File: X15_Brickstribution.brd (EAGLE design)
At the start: 152.4 x 76.2 mm, 87 parts, among them J1 IPL1-104-01-X-S-K, Q1 310mA/60V/1.6Ω, U5 IC_L4970A, U6 DIODE_STPS1545CT, U7 IC_L4970A, U8 DIODE_STPS1545CT

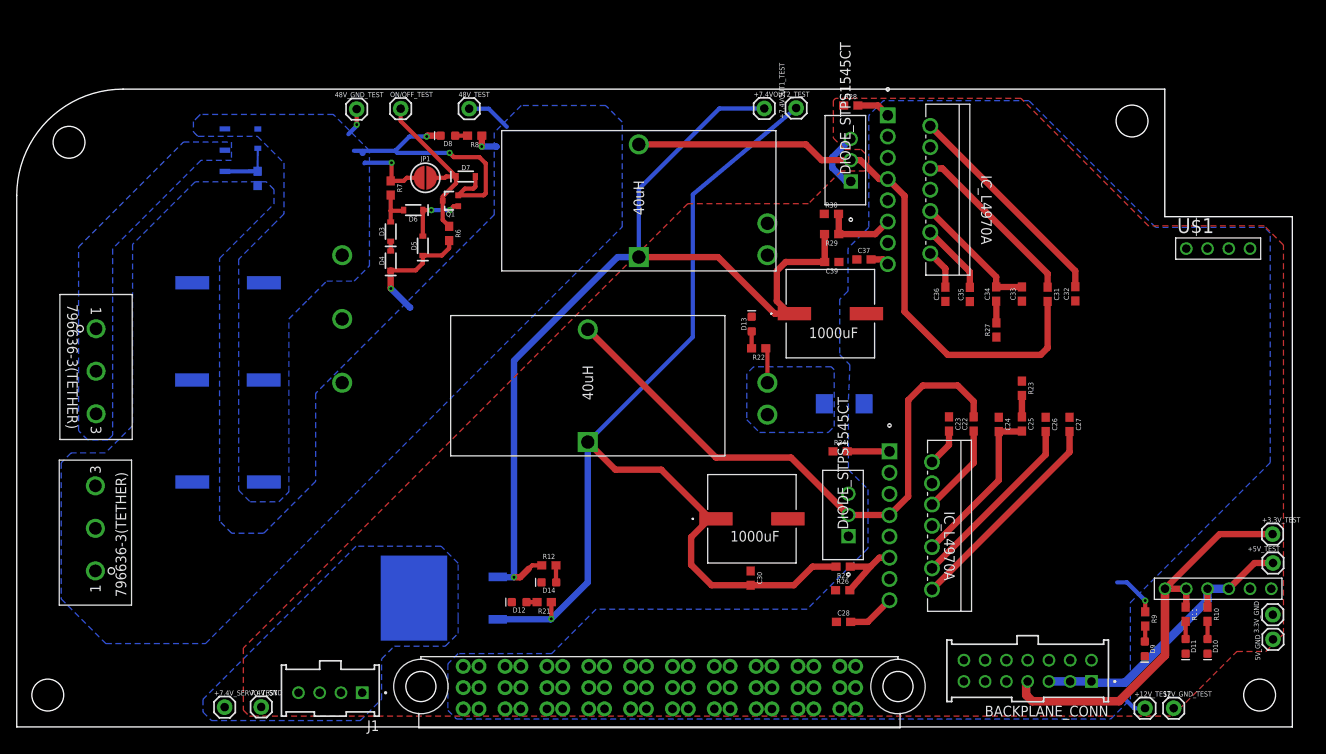
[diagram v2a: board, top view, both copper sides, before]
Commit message: Changed polygons and connections to reference voltage
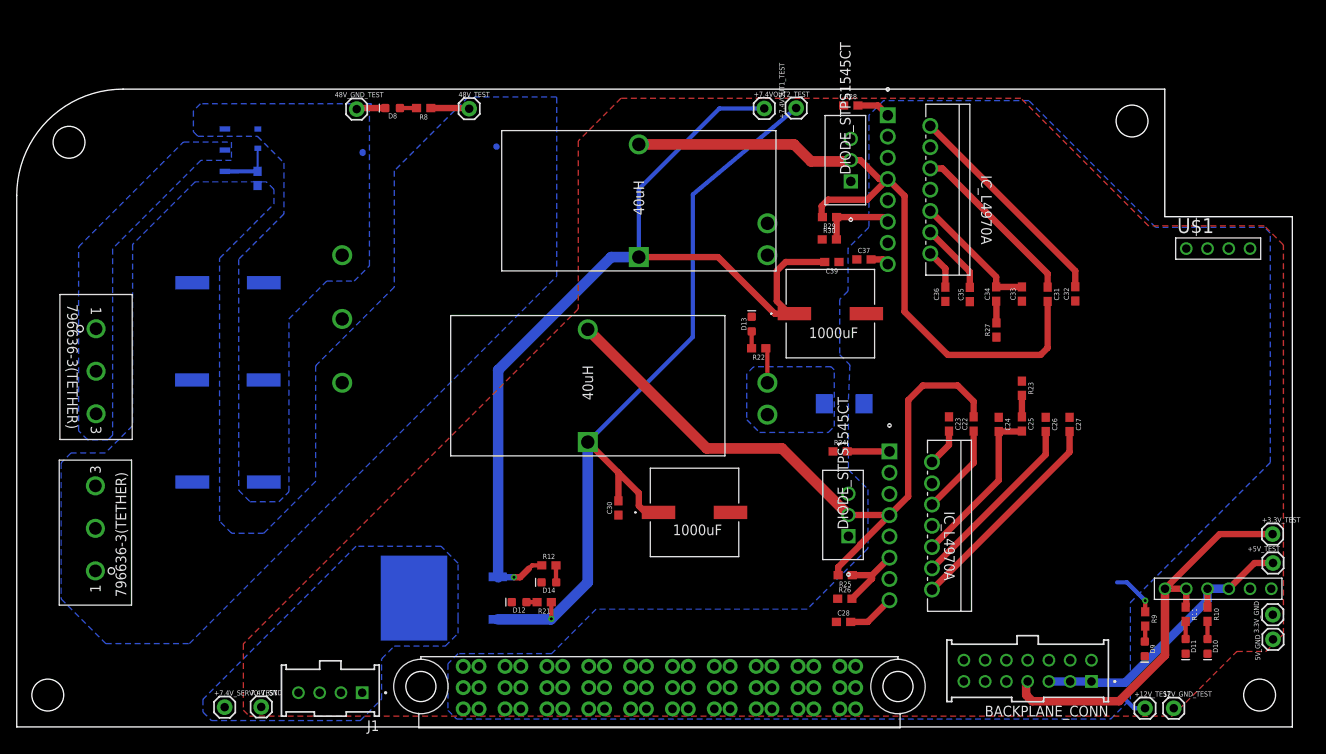
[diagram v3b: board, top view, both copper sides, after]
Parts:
- removed D3, D4: 19V, SparkFun-DiscreteSemi:SOD-323
- removed D5, D6: 250mA/100V, SparkFun-DiscreteSemi:SOD-323
- removed D7: 3.6V, SparkFun-DiscreteSemi:SOD-323
- removed JP1: JUMPER-SMT_2_NO_SILK_ROUND, SparkFun-Jumpers:SMT-JUMPER_2_NO_SILK_ROUND
- removed ON/OFF_TEST: (no value), SparkFun-Connectors:1X01
- removed Q1: 310mA/60V/1.6Ω, SparkFun-DiscreteSemi:SOT323
- removed R6: 10k, SparkFun-Resistors:0603
- removed R7: 1M, SparkFun-Resistors:0603
- moved C30 17.9 mm to (72.0, 26.2), turned to 90 degrees
- moved D8 7.38 mm to (45.0, 73.9)
- moved R8 6.93 mm to (48.7, 73.9)
- moved C29 6.90 mm to (81.1, 25.6)
- moved R30 3.06 mm to (97.2, 58.2)
- moved R29 2.05 mm to (97.2, 60.9)
- moved R25 1.05 mm to (99.1, 18.1)
- moved R26 1.05 mm to (99.0, 15.3)
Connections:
- removed net N$5: D3.C, D4.A
- removed net N$6: D3.A, D6.A, R7.2
- removed net N$7: D5.A, D6.C, Q1.1
- removed net ON/OFF: D7.C, JP1.2, ON/OFF_TEST.1, Q1.3, R6.1
- net +48V: no longer D4.C, D5.C, R6.2
- net 48V_GND: no longer D7.A, JP1.1, Q1.2, R7.1
- net OUT1: now also R25.2
- net OUT2: now also R29.2
- net VOUT1: no longer R25.2
- net VOUT2: no longer R29.2
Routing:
- net 48V_GND: track 45.2 -> 3.57 mm, vias 4 -> 0
- net VOUT1: track 128.0 -> 98.4 mm
- net ON/OFF: track 20.3 -> 0.00 mm
- net +48V: track 23.4 -> 4.65 mm, vias 2 -> 0
- net OUT2: track 73.3 -> 84.0 mm
- net OUT1: track 71.1 -> 80.8 mm
- net N$7: track 7.53 -> 0.00 mm, vias 2 -> 0
- net 12V_GND: track 7.25 -> 0.00 mm
- net N$6: track 4.78 -> 0.00 mm
- net VOUT2: track 116.1 -> 114.0 mm
- net N$5: track 1.18 -> 0.00 mm
- net N$4: track 1.47 -> 1.98 mm
